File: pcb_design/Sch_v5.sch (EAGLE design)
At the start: 30 parts

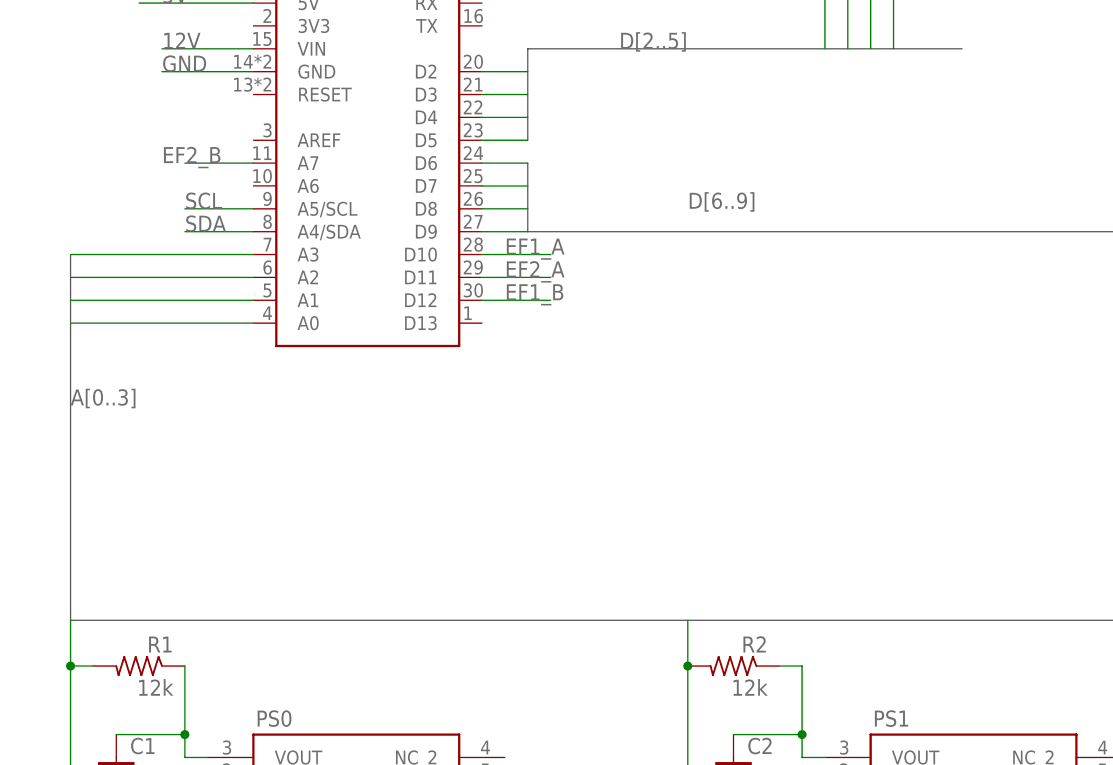
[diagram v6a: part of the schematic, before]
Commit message: added dip switch. autorouting completed
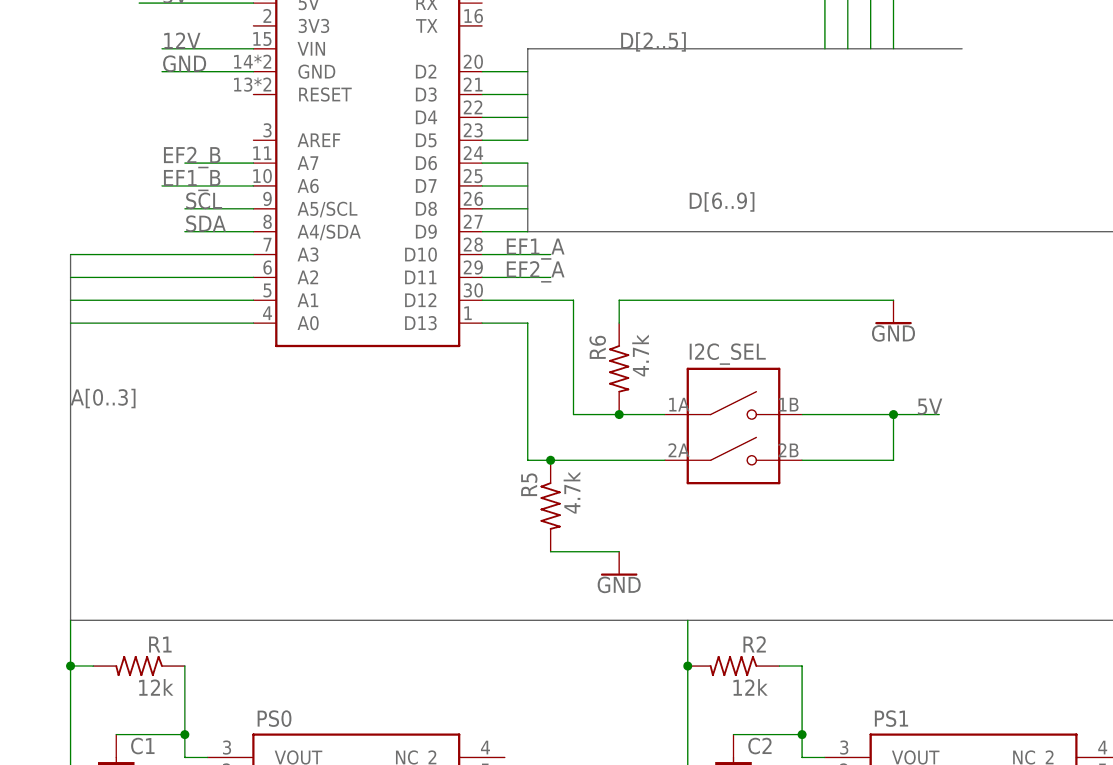
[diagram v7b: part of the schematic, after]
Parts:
- added I2C_SEL: 2PIN_DIP_DS01-254-S-02BE, byu_pressure_control:2PIN_DIP_DS01-254-S-02BE
- added R5, R6: 4.7k, rcl:R-US_0204/7
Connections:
- new net N$13: I2C_SEL.COM1, NANO1.D12, R6.2
- new net N$14: I2C_SEL.COM2, NANO1.D13, R5.1
- net 5V: now also I2C_SEL.NO1, I2C_SEL.NO2
- net EF1_B: now also NANO1.A6; no longer NANO1.D12
- net GND: now also R5.2, R6.1
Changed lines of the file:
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@@
 <clearance class="3" value="0.254"/>
+</class>
+<class number="5" name="Valve Power" width="0.762" drill="0.762">
+<clearance class="3" value="0.508"/>
+<clearance class="4" value="0.508"/>
 </class>
 </classes>
@@
 <part name="I2C_OUT" library="byu_pressure_control" library_urn="urn:adsk.eagle:library:26800355" deviceset="PHOENIX_CONNECTOR_1778625" device="" package3d_urn="urn:adsk.eagle:package:26802270/3"/>
 <part name="NANO1" library="byu_pressure_control" library_urn="urn:adsk.eagle:library:26800355" deviceset="ARDUINO_NANO_EVERY" device="" package3d_urn="urn:adsk.eagle:package:26916803/3"/>
+<part name="I2C_SEL" library="byu_pressure_control" library_urn="urn:adsk.eagle:library:26800355" deviceset="2PIN_DIP_DS01-254-S-02BE" device="" package3d_urn="urn:adsk.eagle:package:26935664/3"/>
+<part name="R5" library="rcl" library_urn="urn:adsk.eagle:library:334" deviceset="R-US_" device="0204/7" package3d_urn="urn:adsk.eagle:package:23498/2" value="4.7k"/>
+<part name="R6" library="rcl" library_urn="urn:adsk.eagle:library:334" deviceset="R-US_" device="0204/7" package3d_urn="urn:adsk.eagle:package:23498/2" value="4.7k"/>
+<part name="GND5" library="SparkFun-PowerSymbols" deviceset="GND" device=""/>
+<part name="GND6" library="SparkFun-PowerSymbols" deviceset="GND" device=""/>
 </parts>
 <sheets>
@@
 <instance part="NANO1" gate="NANO_EVERY" x="35.56" y="101.6" smashed="yes">
 <attribute name="NAME" x="25.4" y="124.968" size="1.778" layer="95" font="vector"/>
+</instance>
+<instance part="I2C_SEL" gate="G$1" x="76.2" y="73.66" smashed="yes">
+<attribute name="NAME" x="71.12" y="82.296" size="1.778" layer="95"/>
+</instance>
+<instance part="R5" gate="G$1" x="55.88" y="66.04" smashed="yes" rot="MR270">
+<attribute name="NAME" x="54.3814" y="69.85" size="1.778" layer="95" rot="MR270"/>
+<attribute name="VALUE" x="59.182" y="69.85" size="1.778" layer="96" rot="MR270"/>
+</instance>
+<instance part="R6" gate="G$1" x="63.5" y="81.28" smashed="yes" rot="MR270">
+<attribute name="NAME" x="62.0014" y="85.09" size="1.778" layer="95" rot="MR270"/>
+<attribute name="VALUE" x="66.802" y="85.09" size="1.778" layer="96" rot="MR270"/>
+</instance>
+<instance part="GND5" gate="1" x="63.5" y="58.42" smashed="yes">
+<attribute name="VALUE" x="63.5" y="58.166" size="1.778" layer="96" align="top-center"/>
+</instance>
+<instance part="GND6" gate="1" x="93.98" y="86.36" smashed="yes">
+<attribute name="VALUE" x="93.98" y="86.106" size="1.778" layer="96" align="top-center"/>
 </instance>
 </instances>
@@
 <wire x1="187.96" y1="104.14" x2="187.96" y2="83.82" width="0.1524" layer="91"/>
 </segment>
-</net>
-<net name="N$1" class="3">
+<segment>
+<pinref part="R5" gate="G$1" pin="2"/>
+<pinref part="GND5" gate="1" pin="GND"/>
+<wire x1="55.88" y1="60.96" x2="63.5" y2="60.96" width="0.1524" layer="91"/>
+</segment>
+<segment>
+<pinref part="R6" gate="G$1" pin="1"/>
+<wire x1="63.5" y1="86.36" x2="63.5" y2="88.9" width="0.1524" layer="91"/>
+<pinref part="GND6" gate="1" pin="GND"/>
+<wire x1="63.5" y1="88.9" x2="93.98" y2="88.9" width="0.1524" layer="91"/>
+</segment>
+</net>
+<net name="N$1" class="0">
 <segment>
 <wire x1="15.24" y1="40.64" x2="7.62" y2="40.64" width="0.1524" layer="91"/>
@@
 </segment>
 </net>
-<net name="N$2" class="3">
+<net name="N$2" class="0">
 <segment>
 <wire x1="83.82" y1="40.64" x2="76.2" y2="40.64" width="0.1524" layer="91"/>
@@
 </segment>
 </net>
-<net name="N$3" class="3">
+<net name="N$3" class="0">
 <segment>
 <wire x1="160.02" y1="40.64" x2="152.4" y2="40.64" width="0.1524" layer="91"/>
@@
 </segment>
 </net>
-<net name="N$4" class="3">
+<net name="N$4" class="0">
 <segment>
 <wire x1="236.22" y1="40.64" x2="228.6" y2="40.64" width="0.1524" layer="91"/>
@@
 <pinref part="C8" gate="G$1" pin="2"/>
 </segment>
+<segment>
+<pinref part="I2C_SEL" gate="G$1" pin="NO1"/>
+<wire x1="83.82" y1="76.2" x2="93.98" y2="76.2" width="0.1524" layer="91"/>
+<pinref part="I2C_SEL" gate="G$1" pin="NO2"/>
+<wire x1="93.98" y1="76.2" x2="99.06" y2="76.2" width="0.1524" layer="91"/>
+<wire x1="83.82" y1="71.12" x2="93.98" y2="71.12" width="0.1524" layer="91"/>
+<wire x1="93.98" y1="71.12" x2="93.98" y2="76.2" width="0.1524" layer="91"/>
+<junction x="93.98" y="76.2"/>
+<label x="96.52" y="76.2" size="1.778" layer="95"/>
+</segment>
 </net>
 <net name="12V" class="2">
@@
 </segment>
 </net>
-<net name="N$6" class="0">
+<net name="N$6" class="5">
 <segment>
 <pinref part="VALVE1" gate="G$1" pin="1"/>
@@
 </segment>
 </net>
-<net name="N$5" class="0">
+<net name="N$5" class="5">
 <segment>
 <pinref part="VALVE1" gate="G$1" pin="2"/>
@@
 </segment>
 </net>
-<net name="N$7" class="0">
+<net name="N$7" class="5">
 <segment>
 <pinref part="VALVE0" gate="G$1" pin="1"/>
@@
 </segment>
 </net>
-<net name="N$8" class="0">
+<net name="N$8" class="5">
 <segment>
 <wire x1="190.5" y1="109.22" x2="190.5" y2="96.52" width="0.1524" layer="91"/>
@@
 </segment>
 <segment>
-<wire x1="48.26" y1="88.9" x2="55.88" y2="88.9" width="0.1524" layer="91"/>
-<label x="50.8" y="88.9" size="1.778" layer="95"/>
-<pinref part="NANO1" gate="NANO_EVERY" pin="D12"/>
+<pinref part="NANO1" gate="NANO_EVERY" pin="A6"/>
+<wire x1="22.86" y1="101.6" x2="12.7" y2="101.6" width="0.1524" layer="91"/>
+<label x="12.7" y="101.6" size="1.778" layer="95"/>
 </segment>
 </net>
@@
 </segment>
 </net>
-<net name="N$10" class="0">
+<net name="N$10" class="5">
 <segment>
 <pinref part="DRIVER_B" gate="G$1" pin="OUT2"/>
@@
 </segment>
 </net>
-<net name="N$9" class="0">
+<net name="N$9" class="5">
 <segment>
 <pinref part="DRIVER_B" gate="G$1" pin="OUT1"/>
@@
 </segment>
 </net>
-<net name="N$11" class="0">
+<net name="N$11" class="5">
 <segment>
 <pinref part="DRIVER_B" gate="G$1" pin="OUT3"/>
@@
 </segment>
 </net>
-<net name="N$12" class="0">
+<net name="N$12" class="5">
 <segment>
 <pinref part="DRIVER_B" gate="G$1" pin="OUT4"/>
@@
 </segment>
 </net>
+<net name="N$13" class="0">
+<segment>
+<pinref part="NANO1" gate="NANO_EVERY" pin="D12"/>
+<wire x1="48.26" y1="88.9" x2="58.42" y2="88.9" width="0.1524" layer="91"/>
+<wire x1="58.42" y1="88.9" x2="58.42" y2="76.2" width="0.1524" layer="91"/>
+<pinref part="I2C_SEL" gate="G$1" pin="COM1"/>
+<wire x1="58.42" y1="76.2" x2="63.5" y2="76.2" width="0.1524" layer="91"/>
+<pinref part="R6" gate="G$1" pin="2"/>
+<wire x1="63.5" y1="76.2" x2="68.58" y2="76.2" width="0.1524" layer="91"/>
+<junction x="63.5" y="76.2"/>
+</segment>
+</net>
+<net name="N$14" class="0">
+<segment>
+<pinref part="NANO1" gate="NANO_EVERY" pin="D13"/>
+<wire x1="48.26" y1="86.36" x2="53.34" y2="86.36" width="0.1524" layer="91"/>
+<wire x1="53.34" y1="86.36" x2="53.34" y2="71.12" width="0.1524" layer="91"/>
+<pinref part="I2C_SEL" gate="G$1" pin="COM2"/>
+<wire x1="53.34" y1="71.12" x2="55.88" y2="71.12" width="0.1524" layer="91"/>
+<pinref part="R5" gate="G$1" pin="1"/>
+<wire x1="55.88" y1="71.12" x2="68.58" y2="71.12" width="0.1524" layer="91"/>
+<junction x="55.88" y="71.12"/>
+</segment>
+</net>
